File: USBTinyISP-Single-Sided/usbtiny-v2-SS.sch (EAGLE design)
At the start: 22 parts, among them IC1 ATTINY2313-20P, IC2 74AHC125N, Q1 12Mhz

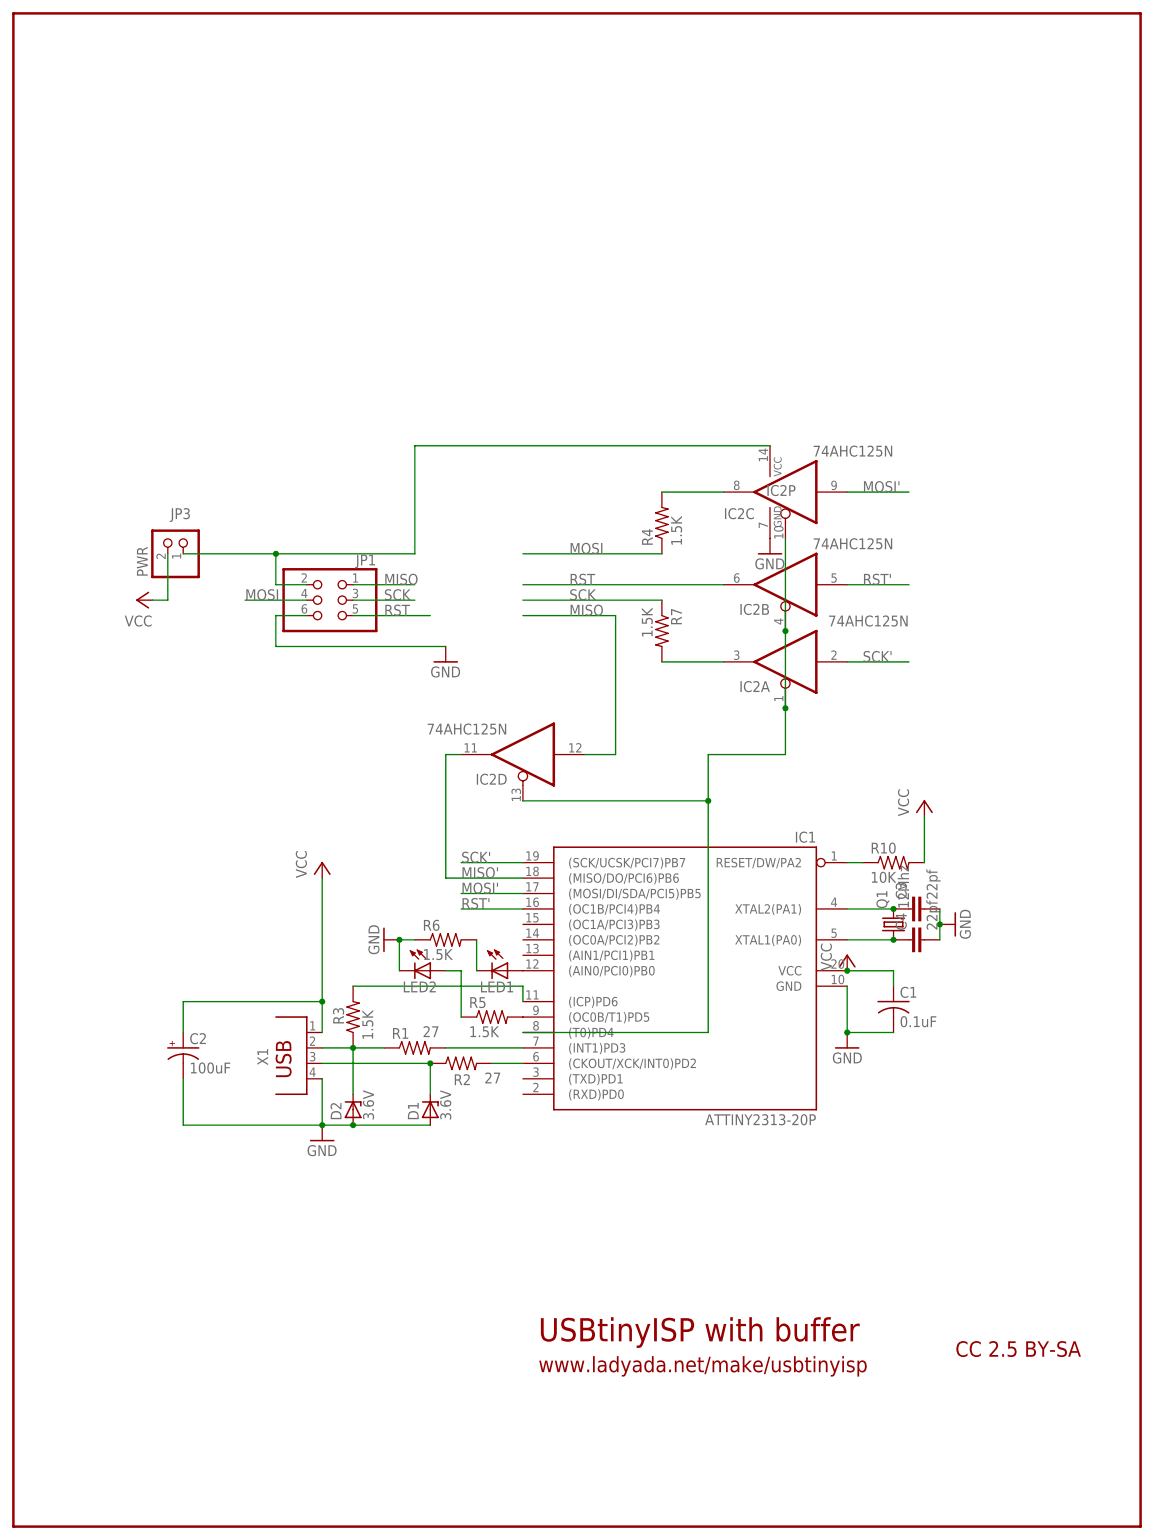
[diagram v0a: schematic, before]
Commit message: Schematic fixes, partial
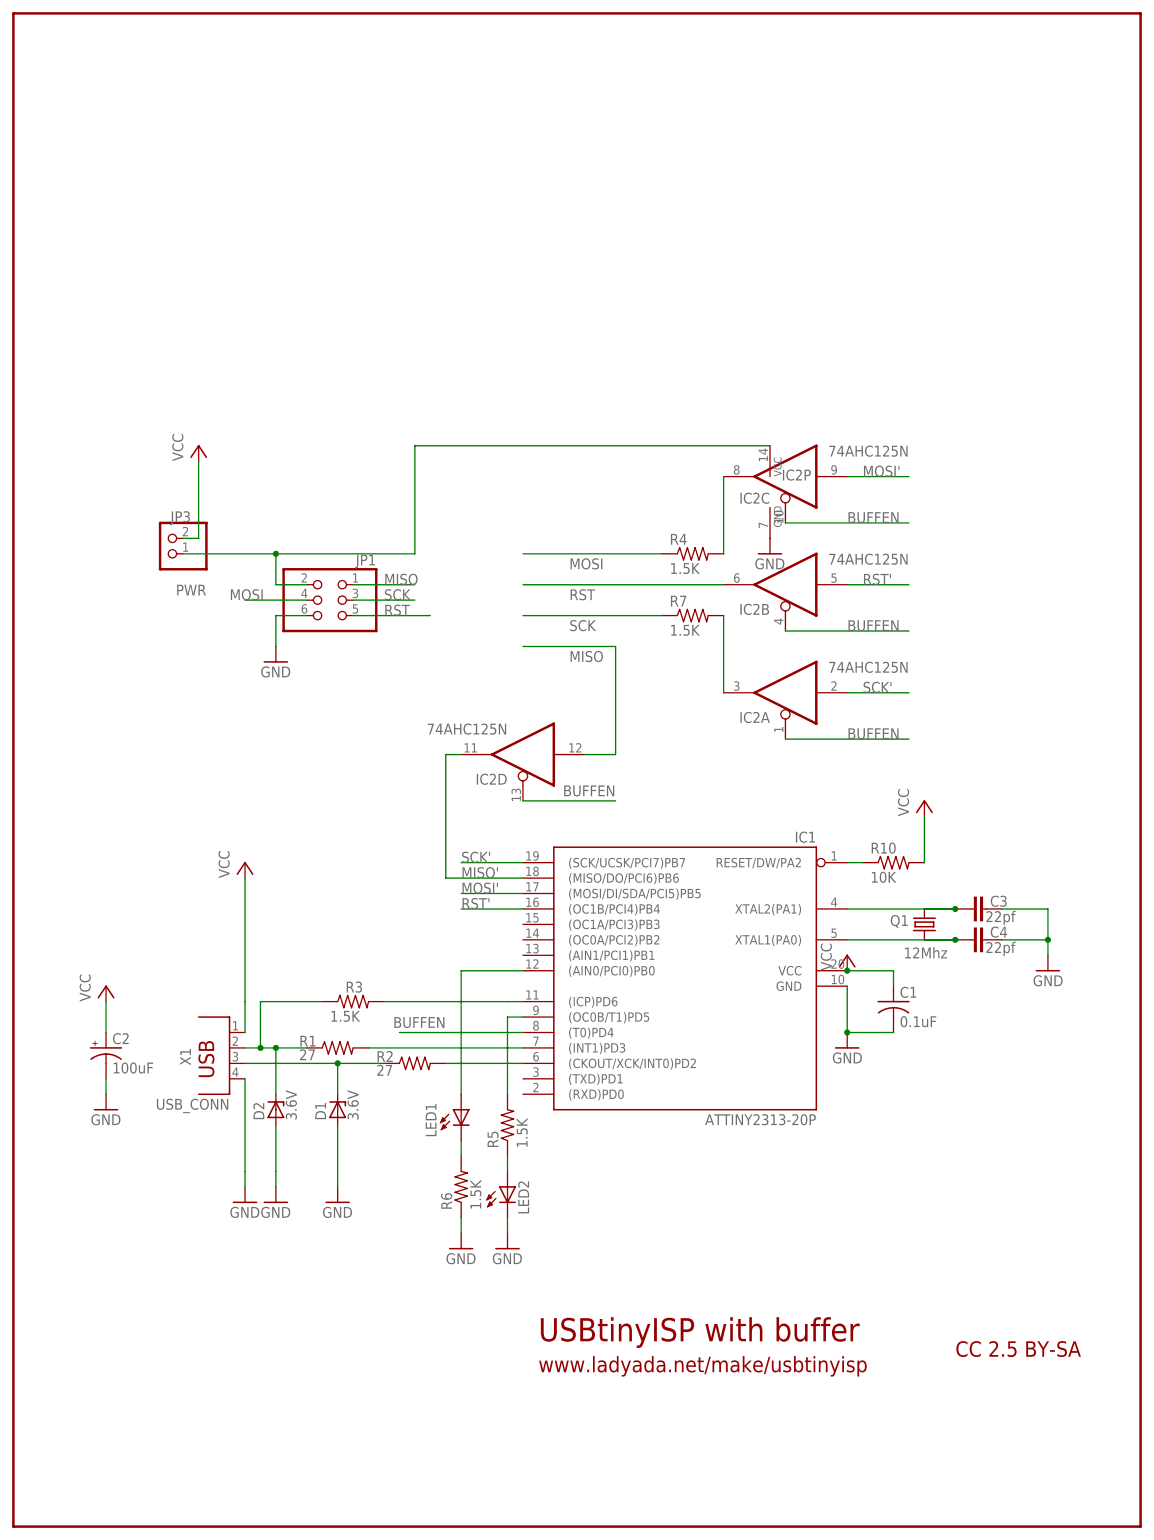
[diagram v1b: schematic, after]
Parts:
- X1: value (none) -> USB_CONN
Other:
- moved on the sheet: C2, C3, C4, D1, D2, IC2A, IC2C, JP3, LED1, LED2, Q1, R1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

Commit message: Version 0.08 - Final tweaks
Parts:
- JP1: value (none) -> ISP_HEADER
- JP3: value PWR -> PWR_JUMPER
- LED1: value (none) -> BURN
- LED2: value (none) -> READY
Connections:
- net N$14 renamed VCC_REMOTE
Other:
- moved on the sheet: C1, IC2P, R4, R7, X1
